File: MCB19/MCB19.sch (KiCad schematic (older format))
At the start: 1 part

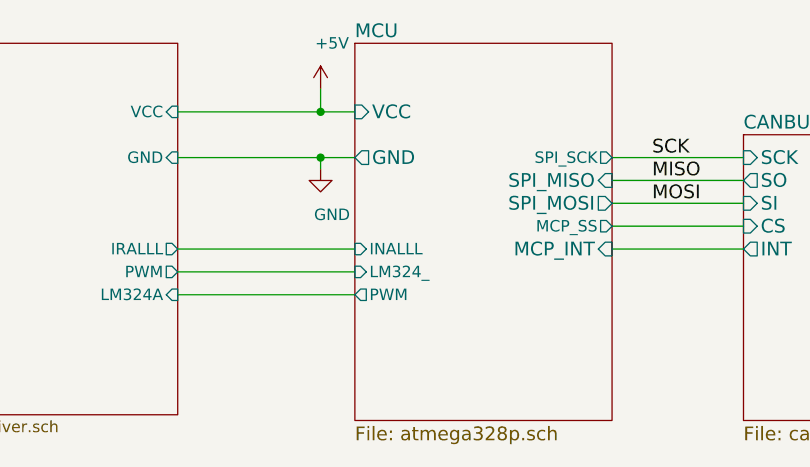
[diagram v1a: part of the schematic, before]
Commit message: Mudanças no layout
Arrumado um problema de portas trocadas
Layout modificado no driver
Proxima parte: Adicionar filtros para as medidas
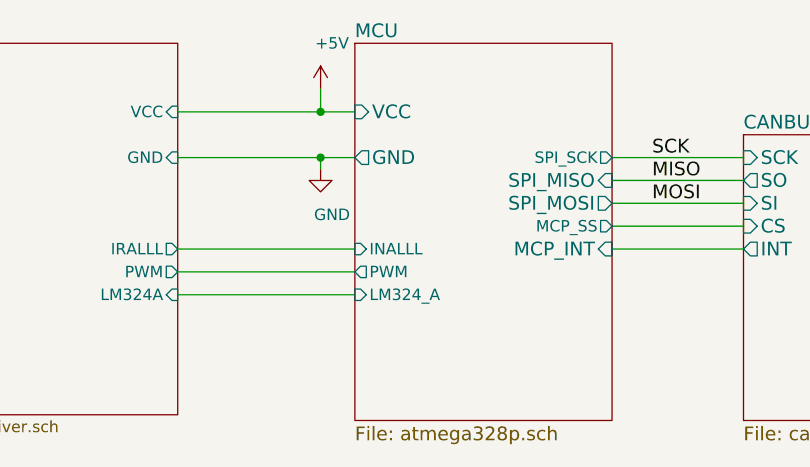
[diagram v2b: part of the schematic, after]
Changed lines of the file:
@@
 F8 "MCP_SS" O R 6725 3150 50
 F9 "INALLL" I L 5600 3250 50
-F10 "LM324_" I L 5600 3350 50
-F11 "PWM" O L 5600 3450 50
+F10 "PWM" O L 5600 3350 50
+F11 "LM324_A" I L 5600 3450 50
 $EndSheet
 $Sheet

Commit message: Final!!!
Pronto para fabricar
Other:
- moved on the sheet: F501
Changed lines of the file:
@@
 $EndDescr
 $Sheet
-S 7300 2750 1350 1250
+S 5550 2750 1350 1250
 U 5AABFC1B
 F0 "CANBUS" 60
 F1 "canbus.sch" 60
-F2 "SI" I L 7300 3050 60
-F3 "SO" O L 7300 2950 60
-F4 "CS" I L 7300 3150 60
-F5 "SCK" I L 7300 2850 60
-F6 "INT" O L 7300 3250 60
-F7 "GND" O R 8650 2900 60
-F8 "VCC" I R 8650 2800 60
-F9 "CAN_H" B R 8650 3000 60
-F10 "CAN_L" B R 8650 3100 60
-$EndSheet
-$Sheet
-S 7175 875  1050 500
+F2 "SI" I R 6900 3050 60
+F3 "SO" O R 6900 2950 60
+F4 "CS" I R 6900 3150 60
+F5 "SCK" I R 6900 2850 60
+F6 "INT" O R 6900 3250 60
+F7 "GND" O L 5550 2900 60
+F8 "VCC" I L 5550 2800 60
+F9 "CAN_H" B L 5550 3000 60
+F10 "CAN_L" B L 5550 3100 60
+$EndSheet
+$Sheet
+S 5975 875  1050 500
 U 5AACFFEF
 F0 "POWER SUPPLY" 60
 F1 "supplies.sch" 60
-F2 "GND" O R 8225 1175 60
-F3 "+5V_OUT" O L 7175 1175 60
-F4 "+18V_IN" I R 8225 1075 60
-$EndSheet
-$Sheet
-S 9675 1025 600  450
+F2 "GND" O L 5975 1175 60
+F3 "+5V_OUT" O R 7025 1175 60
+F4 "+18V_IN" I L 5975 1075 60
+$EndSheet
+$Sheet
+S 3925 1025 600  450
 U 5AAD16DD
 F0 "CANBUS CONN" 60
 F1 "canbus_connector.sch" 60
-F2 "CAN_H" B L 9675 1275 60
-F3 "CAN_L" B L 9675 1375 60
-F4 "CAN_18V" O L 9675 1075 60
-F5 "CAN_GND" B L 9675 1175 60
-$EndSheet
-Text Label 6900 3050 0    60   ~ 0
+F2 "CAN_H" B R 4525 1275 60
+F3 "CAN_L" B R 4525 1375 60
+F4 "CAN_18V" O R 4525 1075 60
+F5 "CAN_GND" B R 4525 1175 60
+$EndSheet
+Text Label 7300 3050 2    60   ~ 0
 MOSI
-Text Label 6900 2950 0    60   ~ 0
+Text Label 7300 2950 2    60   ~ 0
 MISO
-Text Label 6900 2850 0    60   ~ 0
+Text Label 7300 2850 2    60   ~ 0
 SCK
 Wire Wire Line
-	9675 1275 9375 1275
-Wire Wire Line
-	8650 3100 9475 3100
-Wire Wire Line
-	9475 1375 9675 1375
-Connection ~ 9275 1175
-Wire Wire Line
-	7175 1175 6975 1175
-Wire Wire Line
-	8850 2800 8650 2800
-Wire Wire Line
-	9275 1175 9675 1175
+	4525 1275 4825 1275
+Wire Wire Line
+	5550 3100 4725 3100
+Wire Wire Line
+	4725 1375 4525 1375
+Connection ~ 4925 1175
+Wire Wire Line
+	7025 1175 7225 1175
+Wire Wire Line
+	5350 2800 5550 2800
+Wire Wire Line
+	4925 1175 4525 1175
 $Comp
 L power:+5V #PWR0105
 U 1 1 5BE8FCAE
-P 8850 2700
-F 0 "#PWR0105" H 8850 2550 50  0001 C CNN
-F 1 "+5V" H 8900 2900 50  0000 C CNN
-F 2 "" H 8850 2700 50  0001 C CNN
-F 3 "" H 8850 2700 50  0001 C CNN
-	1    8850 2700
-	1    0    0    -1
+P 5350 2700
+F 0 "#PWR0105" H 5350 2550 50  0001 C CNN
+F 1 "+5V" H 5400 2900 50  0000 C CNN
+F 2 "" H 5350 2700 50  0001 C CNN
+F 3 "" H 5350 2700 50  0001 C CNN
+	1    5350 2700
+	-1   0    0    -1
 $EndComp
 $Comp
 L power:+5V #PWR0104
 U 1 1 5C9032F1
-P 5450 2550
-F 0 "#PWR0104" H 5450 2400 50  0001 C CNN
-F 1 "+5V" H 5500 2750 50  0000 C CNN
-F 2 "" H 5450 2550 50  0001 C CNN
-F 3 "" H 5450 2550 50  0001 C CNN
-	1    5450 2550
-	1    0    0    -1
-$EndComp
-Wire Wire Line
-	5450 2550 5450 2650
-Wire Wire Line
-	5450 2650 5600 2650
+P 8750 2550
+F 0 "#PWR0104" H 8750 2400 50  0001 C CNN
+F 1 "+5V" H 8800 2750 50  0000 C CNN
+F 2 "" H 8750 2550 50  0001 C CNN
+F 3 "" H 8750 2550 50  0001 C CNN
+	1    8750 2550
+	-1   0    0    -1
+$EndComp
+Wire Wire Line
+	8750 2550 8750 2650
+Wire Wire Line
+	8750 2650 8600 2650
 $Comp
 L power:GND #PWR0106
 U 1 1 5C9038CC
-P 5450 2900
-F 0 "#PWR0106" H 5450 2650 50  0001 C CNN
-F 1 "GND" H 5500 2700 50  0000 C CNN
-F 2 "" H 5450 2900 50  0001 C CNN
-F 3 "" H 5450 2900 50  0001 C CNN
-	1    5450 2900
-	1    0    0    -1
-$EndComp
-Wire Wire Line
-	5450 2900 5450 2850
-Wire Wire Line
-	5450 2850 5600 2850
+P 8750 2900
+F 0 "#PWR0106" H 8750 2650 50  0001 C CNN
+F 1 "GND" H 8800 2700 50  0000 C CNN
+F 2 "" H 8750 2900 50  0001 C CNN
+F 3 "" H 8750 2900 50  0001 C CNN
+	1    8750 2900
+	-1   0    0    -1
+$EndComp
+Wire Wire Line
+	8750 2900 8750 2850
+Wire Wire Line
+	8750 2850 8600 2850
 $Comp
 L power:+5V #PWR0102
 U 1 1 5CDDDD31
-P 6975 1175
-F 0 "#PWR0102" H 6975 1025 50  0001 C CNN
-F 1 "+5V" H 7025 1375 50  0000 C CNN
-F 2 "" H 6975 1175 50  0001 C CNN
-F 3 "" H 6975 1175 50  0001 C CNN
-	1    6975 1175
-	1    0    0    -1
+P 7225 1175
+F 0 "#PWR0102" H 7225 1025 50  0001 C CNN
+F 1 "+5V" H 7275 1375 50  0000 C CNN
+F 2 "" H 7225 1175 50  0001 C CNN
+F 3 "" H 7225 1175 50  0001 C CNN
+	1    7225 1175
+	-1   0    0    -1
 $EndComp
 $Comp
 L power:GND #PWR0103
 U 1 1 5CDE058E
-P 9125 2250
-F 0 "#PWR0103" H 9125 2000 50  0001 C CNN
-F 1 "GND" H 9130 2077 50  0000 C CNN
-F 2 "" H 9125 2250 50  0001 C CNN
-F 3 "" H 9125 2250 50  0001 C CNN
-	1    9125 2250
-	1    0    0    -1
-$EndComp
-Wire Wire Line
-	9125 2250 9125 2175
-Wire Wire Line
-	9125 2175 9275 2175
-Wire Wire Line
-	8850 2700 8850 2800
-Wire Wire Line
-	9275 2175 9275 2900
-Connection ~ 9275 2175
-Wire Wire Line
-	8650 2900 9275 2900
-Wire Wire Line
-	9375 1275 9375 3000
-Wire Wire Line
-	9375 3000 8650 3000
-Wire Wire Line
-	9475 1375 9475 3100
-Wire Wire Line
-	8225 1175 9275 1175
+P 5075 2250
+F 0 "#PWR0103" H 5075 2000 50  0001 C CNN
+F 1 "GND" H 5080 2077 50  0000 C CNN
+F 2 "" H 5075 2250 50  0001 C CNN
+F 3 "" H 5075 2250 50  0001 C CNN
+	1    5075 2250
+	-1   0    0    -1
+$EndComp
+Wire Wire Line
+	5075 2250 5075 2175
+Wire Wire Line
+	5075 2175 4925 2175
+Wire Wire Line
+	5350 2700 5350 2800
+Wire Wire Line
+	4925 2175 4925 2900
+Connection ~ 4925 2175
+Wire Wire Line
+	5550 2900 4925 2900
+Wire Wire Line
+	4825 1275 4825 3000
+Wire Wire Line
+	4825 3000 5550 3000
+Wire Wire Line
+	4725 1375 4725 3100
+Wire Wire Line
+	5975 1175 4925 1175
 $Comp
 L Device:Fuse_Small F501
 U 1 1 5CDF621D
-P 9450 1075
-F 0 "F501" H 9450 1260 50  0000 C CNN
-F 1 "500mA" H 9450 1169 50  0000 C CNN
-F 2 "Fuse:Fuse_1206_3216Metric_Pad1.42x1.75mm_HandSolder" H 9450 1075 50  0001 C CNN
-F 3 "~" H 9450 1075 50  0001 C CNN
-	1    9450 1075
-	1    0    0    -1
-$EndComp
-Wire Wire Line
-	9550 1075 9675 1075
-Wire Wire Line
-	6725 2850 7300 2850
-Wire Wire Line
-	6725 2950 7300 2950
-Wire Wire Line
-	6725 3050 7300 3050
-Wire Wire Line
-	6725 3150 7300 3150
-Wire Wire Line
-	6725 3250 7300 3250
-$Sheet
-S 5600 2350 1125 1650
+P 4750 1075
+F 0 "F501" H 4750 1260 50  0000 C CNN
+F 1 "500mA" H 4750 1169 50  0000 C CNN
+F 2 "Fuse:Fuse_1206_3216Metric_Pad1.42x1.75mm_HandSolder" H 4750 1075 50  0001 C CNN
+F 3 "~" H 4750 1075 50  0001 C CNN
+	1    4750 1075
+	-1   0    0    -1
+$EndComp
+Wire Wire Line
+	4650 1075 4525 1075
+Wire Wire Line
+	7475 2850 6900 2850
+Wire Wire Line
+	7475 2950 6900 2950
+Wire Wire Line
+	7475 3050 6900 3050
+Wire Wire Line
+	7475 3150 6900 3150
+Wire Wire Line
+	7475 3250 6900 3250
+$Sheet
+S 7475 2350 1125 1650
 U 5AACA401
 F0 "MCU" 60
 F1 "atmega328p.sch" 60
-F2 "SPI_MISO" I R 6725 2950 60
-F3 "SPI_MOSI" O R 6725 3050 60
-F4 "MCP_INT" I R 6725 3250 60
-F5 "VCC" I L 5600 2650 60
-F6 "GND" O L 5600 2850 60
-F7 "SPI_SCK" O R 6725 2850 50
-F8 "MCP_SS" O R 6725 3150 50
-F9 "INALLL" I L 5600 3250 50
-F10 "PWM" O L 5600 3350 50
-F11 "LM324_A" I L 5600 3450 50
-$EndSheet
-$Sheet
-S 3800 2350 1025 1625
+F2 "SPI_MISO" I L 7475 2950 60
+F3 "SPI_MOSI" O L 7475 3050 60
+F4 "MCP_INT" I L 7475 3250 60
+F5 "VCC" I R 8600 2650 60
+F6 "GND" O R 8600 2850 60
+F7 "SPI_SCK" O L 7475 2850 50
+F8 "MCP_SS" O L 7475 3150 50
+F9 "INALLL" I R 8600 3250 50
+F10 "PWM" O R 8600 3350 50
+F11 "LM324_A" I R 8600 3450 50
+$EndSheet
+$Sheet
+S 9375 2350 1025 1625
 U 5D414D87
 F0 "driver" 50
 F1 "driver.sch" 50
-F2 "VCC" I R 4825 2650 50
-F3 "GND" I R 4825 2850 50
-F4 "IRALLL" O R 4825 3250 50
-F5 "PWM" O R 4825 3350 50
-F6 "LM324A" I R 4825 3450 50
-$EndSheet
-Wire Wire Line
-	9275 1175 9275 2175
-Wire Wire Line
-	8225 1075 9350 1075
-Wire Wire Line
-	4825 3250 5600 3250
-Wire Wire Line
-	5600 3350 4825 3350
-Wire Wire Line
-	5600 3450 4825 3450
-Wire Wire Line
-	5450 2850 4825 2850
-Connection ~ 5450 2850
-Wire Wire Line
-	4825 2650 5450 2650
-Connection ~ 5450 2650
+F2 "VCC" I L 9375 2650 50
+F3 "GND" I L 9375 2850 50
+F4 "IRALLL" O L 9375 3250 50
+F5 "PWM" O L 9375 3350 50
+F6 "LM324A" I L 9375 3450 50
+$EndSheet
+Wire Wire Line
+	4925 1175 4925 2175
+Wire Wire Line
+	5975 1075 4850 1075
+Wire Wire Line
+	9375 3250 8600 3250
+Wire Wire Line
+	8600 3350 9375 3350
+Wire Wire Line
+	8600 3450 9375 3450
+Wire Wire Line
+	8750 2850 9375 2850
+Connection ~ 8750 2850
+Wire Wire Line
+	9375 2650 8750 2650
+Connection ~ 8750 2650
 $EndSCHEMATC

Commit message: New version
Detalhes
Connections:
- net labels added: +15V
- wire segments 32 -> 39
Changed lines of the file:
@@
 $Descr A4 11693 8268
 encoding utf-8
-Sheet 1 6
+Sheet 1 7
 Title ""
 Date ""
@@
 Wire Wire Line
 	4725 1375 4525 1375
-Connection ~ 4925 1175
 Wire Wire Line
 	7025 1175 7225 1175
@@
 F5 "PWM" O L 9375 3350 50
 F6 "LM324A" I L 9375 3450 50
-$EndSheet
-Wire Wire Line
-	4925 1175 4925 2175
-Wire Wire Line
-	5975 1075 4850 1075
+F7 "+15V" I L 9375 2450 50
+$EndSheet
+Wire Wire Line
+	4925 1175 4925 1850
+Wire Wire Line
+	5975 1075 5025 1075
 Wire Wire Line
 	9375 3250 8600 3250
@@
 	9375 2650 8750 2650
 Connection ~ 8750 2650
+Connection ~ 4925 1175
+Wire Wire Line
+	5975 1850 4925 1850
+Connection ~ 4925 1850
+Wire Wire Line
+	4925 1850 4925 2175
+Wire Wire Line
+	5975 1750 5025 1750
+Wire Wire Line
+	5025 1750 5025 1075
+Connection ~ 5025 1075
+Wire Wire Line
+	5025 1075 4850 1075
+$Comp
+L power:+15V #PWR0109
+U 1 1 5D9C5743
+P 7225 1850
+F 0 "#PWR0109" H 7225 1700 50  0001 C CNN
+F 1 "+15V" H 7240 2023 50  0000 C CNN
+F 2 "" H 7225 1850 50  0001 C CNN
+F 3 "" H 7225 1850 50  0001 C CNN
+	1    7225 1850
+	1    0    0    -1
+$EndComp
+Wire Wire Line
+	7025 1850 7225 1850
+$Comp
+L power:+15V #PWR0112
+U 1 1 5DA06051
+P 9175 2450
+F 0 "#PWR0112" H 9175 2300 50  0001 C CNN
+F 1 "+15V" H 9190 2623 50  0000 C CNN
+F 2 "" H 9175 2450 50  0001 C CNN
+F 3 "" H 9175 2450 50  0001 C CNN
+	1    9175 2450
+	1    0    0    -1
+$EndComp
+Wire Wire Line
+	9175 2450 9375 2450
+$Sheet
+S 5975 1525 1050 500
+U 5DA09AB7
+F0 "supplies15" 50
+F1 "+15V.sch" 50
+F2 "GND" O L 5975 1850 50
+F3 "+15V_OUT" I R 7025 1850 50
+F4 "+18V_IN" I L 5975 1750 50
+$EndSheet
 $EndSCHEMATC
